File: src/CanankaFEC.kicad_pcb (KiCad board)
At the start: 2 copper layers, 24 x 27.9 mm, 27 parts, among them J1 105444-0001, J2 B3B-XH-A, U1 FT232RL, U2 PIC18F25K80, U3 MCP2561

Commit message: Added transistor models
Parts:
- Q1, Q2, Q3: value (none) -> BSS84
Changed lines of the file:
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@@
 			)
 		)
-		(property "Value" ""
+		(property "Value" "BSS84"
 			(at 0 -2.5 0)
 			(layer "B.SilkS")
@@
 			)
 		)
-		(property "Value" ""
+		(property "Value" "BSS84"
 			(at 0 -2.5 0)
 			(layer "B.SilkS")
@@
 			)
 		)
-		(property "Value" ""
+		(property "Value" "BSS84"
 			(at 0 -2.5 0)
 			(layer "B.SilkS")

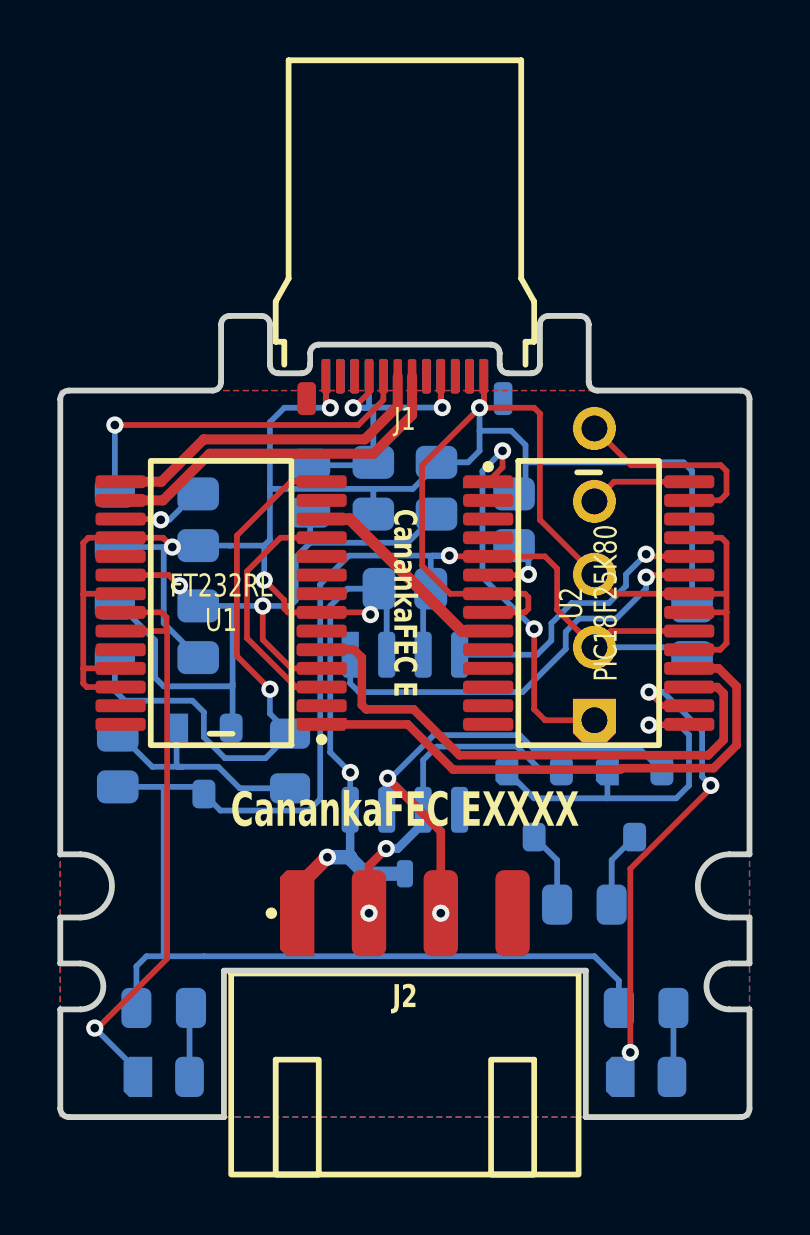
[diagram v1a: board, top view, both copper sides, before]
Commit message: Fixed termination mosfet setup
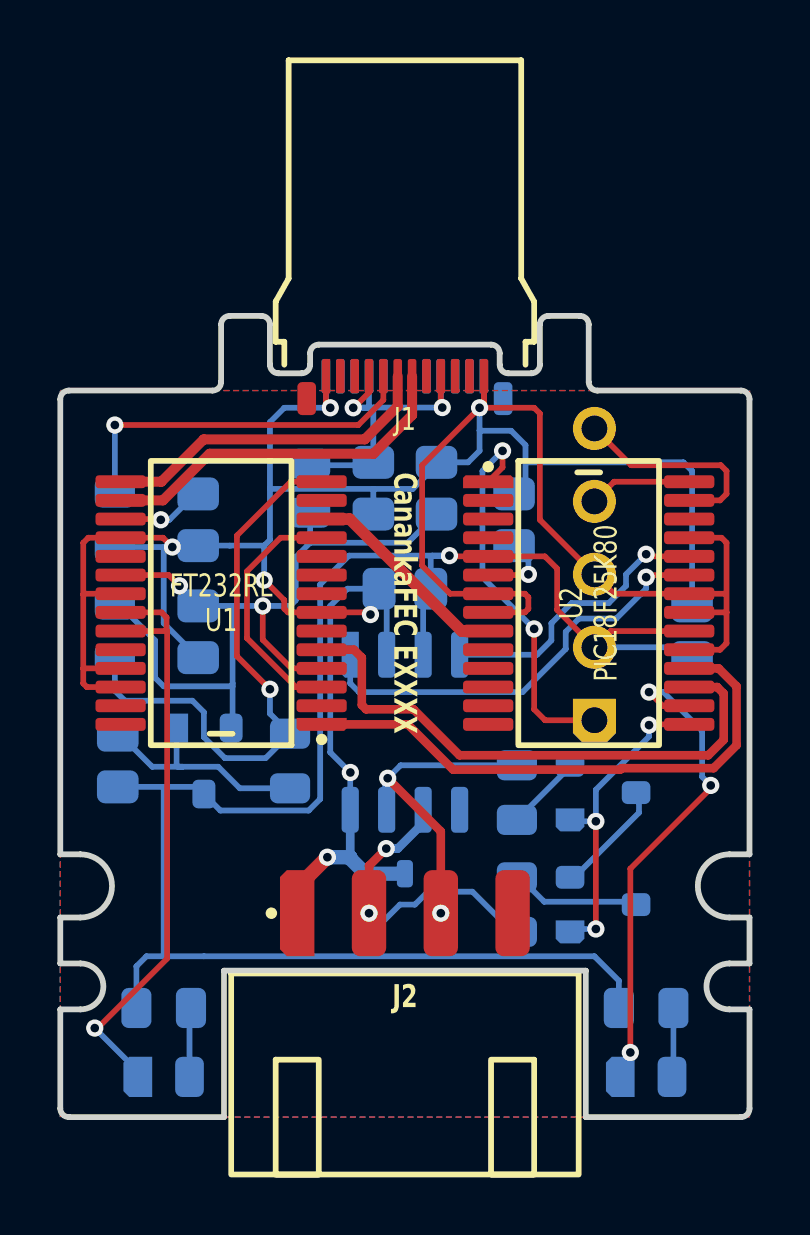
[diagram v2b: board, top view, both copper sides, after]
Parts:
- added R2: 59, Medo64:R (0805), B.Cu at (35.9, 40.5)
- R1: value 118 -> 59
- moved R1 4.55 mm to (35.9, 36.6), turned to 90 degrees
- moved Q3 3.67 mm to (38.9, 40.5), turned to 90 degrees
- moved Q2 2.43 mm to (38.9, 36.6), turned to 90 degrees
- renumbered R2 to R3, R3 to R4, R4 to R5, R5 to R6
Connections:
- net TERMINATE renamed IO_CONTROL_TERMINATE#
- D1 pad 1: CANH -> CAN_H
- D1 pad 2: CANL -> CAN_L
- J2 pad 2: CANL -> CAN_L
- J2 pad 3: CANH -> CAN_H
- Q2 pad 2: CANL -> CAN_H_TERM
- Q2 pad 3: CAN_L_TERM -> CAN_I_TERM
- Q3 pad 2: CANH -> CAN_I_TERM
- Q3 pad 3: CAN_H_TERM -> CAN_L_TERM
- R1 pad 1: CAN_L_TERM -> CAN_H_TERM
- R1 pad 2: CAN_H_TERM -> CAN_H
- U3 pad 6: CANL -> CAN_L
- U3 pad 7: CANH -> CAN_H
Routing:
- net CANH: track 19.3 -> 0.00 mm, vias 2 -> 0
- net CAN_H: track 0.00 -> 13.2 mm, vias 0 -> 2
- net CANL: track 11.7 -> 0.00 mm, vias 2 -> 0
- net CAN_L: track 0.00 -> 11.1 mm, vias 0 -> 2
- net CAN_I_TERM: track 0.00 -> 3.69 mm
- net CAN_L_TERM: track 2.68 -> 4.40 mm
- net IO_CONTROL_TERMINATE#: track 12.6 -> 11.0 mm, vias 1 -> 3
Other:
- board text removed: "CanankaFEC E"

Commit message: Consolidating resistors a bit
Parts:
- R6: value 10K -> 5K1
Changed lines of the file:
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@@
 			)
 		)
-		(property "Value" "10K"
+		(property "Value" "5K1"
 			(at 2.3 0 0)
 			(layer "B.SilkS")

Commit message: Added pin silkscreen
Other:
- board text added: "GND"
- board text added: "H"
- board text added: "L"
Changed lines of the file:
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@@
+		)
+	)
+	(gr_text "H"
+		(at 33.2 37.5 0)
+		(layer "F.SilkS" knockout)
+		(effects
+			(font
+				(size 1.1 0.7)
+				(thickness 0.15)
+				(bold yes)
+			)
+		)
+	)
+	(gr_text "GND"
+		(at 28.2 37.5 0)
+		(layer "F.SilkS" knockout)
+		(effects
+			(font
+				(size 1.1 0.7)
+				(thickness 0.15)
+				(bold yes)
+			)
+		)
+	)
+	(gr_text "L"
+		(at 30.7 37.5 0)
+		(layer "F.SilkS" knockout)
+		(effects
+			(font
+				(size 1.1 0.7)
+				(thickness 0.15)
+				(bold yes)
+			)
 		)
 	)
